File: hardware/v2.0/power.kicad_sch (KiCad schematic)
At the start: 48 parts, among them U1 ECP5-CABGA256, U2 TLV62569DBV, U3 TLV62569DBV, U4 TLV62569DBV

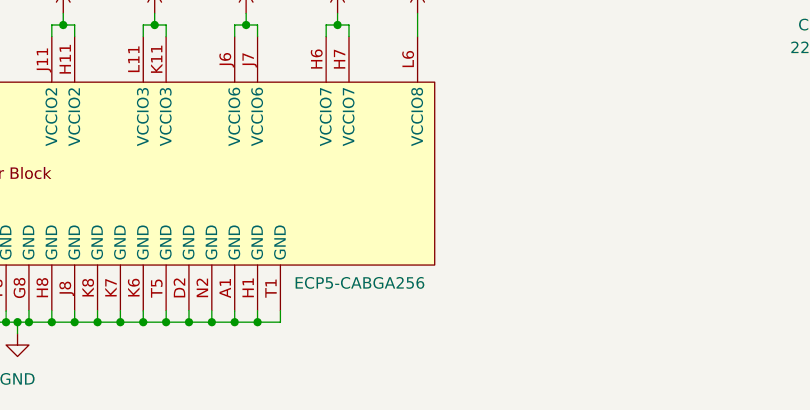
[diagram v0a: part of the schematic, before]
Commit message: Initial plan for adding an external ADC
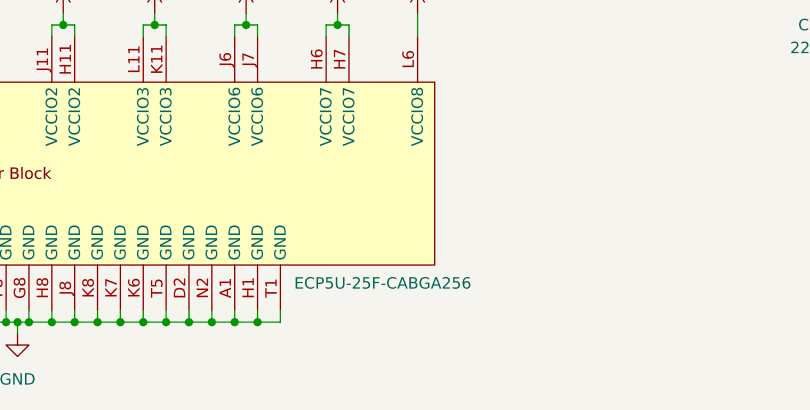
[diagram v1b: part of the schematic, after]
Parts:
- U1: value ECP5-CABGA256 -> ECP5U-25F-CABGA256; LCSC Link https://lcsc.com/product-detail/Programmable-Logic-Device-C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 -> (none); LCSC Part # C1521614 -> (none); Manufactuer Part Number LFE5U-25F-6BG256C -> (none)
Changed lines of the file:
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@@
 			)
 		)
-		(property "Value" "ECP5-CABGA256"
+		(property "Value" "ECP5U-25F-CABGA256"
 			(at 132.334 154.432 0)
 			(effects
@@
 			(effects
 				(font
-					(size 1.27 1.27)
-				)
-				(hide yes)
-			)
-		)
-		(property "LCSC Link" "https://lcsc.com/product-detail/Programmable-Logic-Device-CPLDs-FPGAs_Lattice-LFE5U-25F-6BG256C_C1521614.html"
-			(at 100.33 142.24 0)
-			(effects
-				(font
-					(size 1.27 1.27)
-				)
-				(hide yes)
-			)
-		)
-		(property "Manufactuer Part Number" "LFE5U-25F-6BG256C"
-			(at 100.33 142.24 0)
-			(effects
-				(font
-					(size 1.27 1.27)
-				)
-				(hide yes)
-			)
-		)
-		(property "LCSC Part #" "C1521614"
-			(at 100.33 142.24 0)
-			(effects
-				(font
-					(size 1.27 1.27)
-				)
-				(hide yes)
-			)
-		)
-		(property "Note" ""
-			(at 100.33 142.24 0)
-			(effects
-				(font
-					(size 1.27 1.27)
-				)
-				(hide yes)
-			)
-		)
-		(property "Notes" ""
-			(at 100.33 142.24 0)
-			(effects
-				(font
